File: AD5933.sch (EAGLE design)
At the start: 80 parts, among them U1 ADG1604BRUZ, U10 ADP3303ARZ-3.3, U11 AD5242BRZ1M, U12 AD5245BRJZ100-R2, U2 AD5933YRSZ, U3 AD5242BRZ1M, U4 AD8606ARZ, U5 ADG1604BRUZ, U7 AD8606ARZ, U8 LTC6904MPMS8TRPBF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

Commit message: complete DRC in layout
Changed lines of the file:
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@@
 <class number="0" name="default" width="0" drill="0.3048">
 </class>
-<class number="1" name="power 5v" width="0.508" drill="0.6096">
+<class number="1" name="power 5v" width="0.4064" drill="0.6096">
 </class>
 </classes>
@@
 </nets>
 </sheet>
-<sheet>
-<plain>
-</plain>
-<instances>
-</instances>
-<busses>
-</busses>
-<nets>
-</nets>
-</sheet>

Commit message: Modify top silk screen, estimate wirelength
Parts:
- renumbered ANALOG_PWR to APWR, DIGITAL_PWR to DPWR, JP1 to Z, JP4 to PWR_SEL

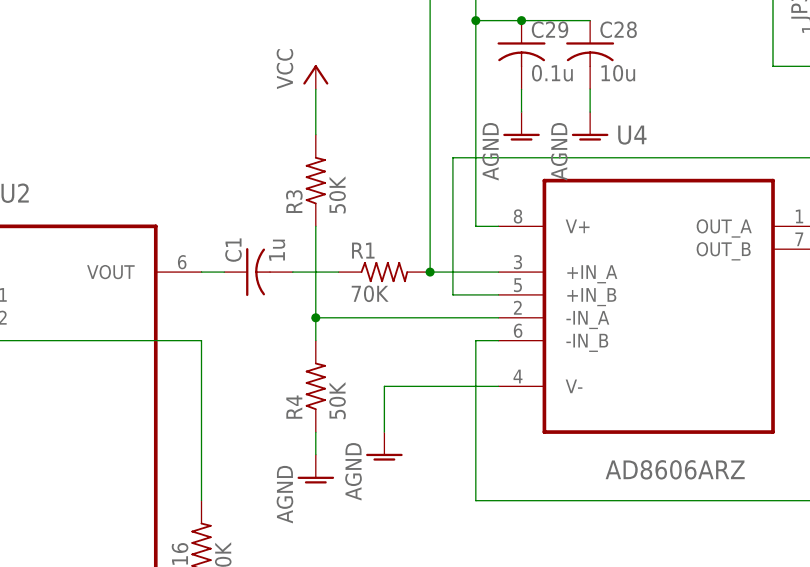
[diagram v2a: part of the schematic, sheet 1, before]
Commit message: Fix ad8606 wiring bug rev 1.1
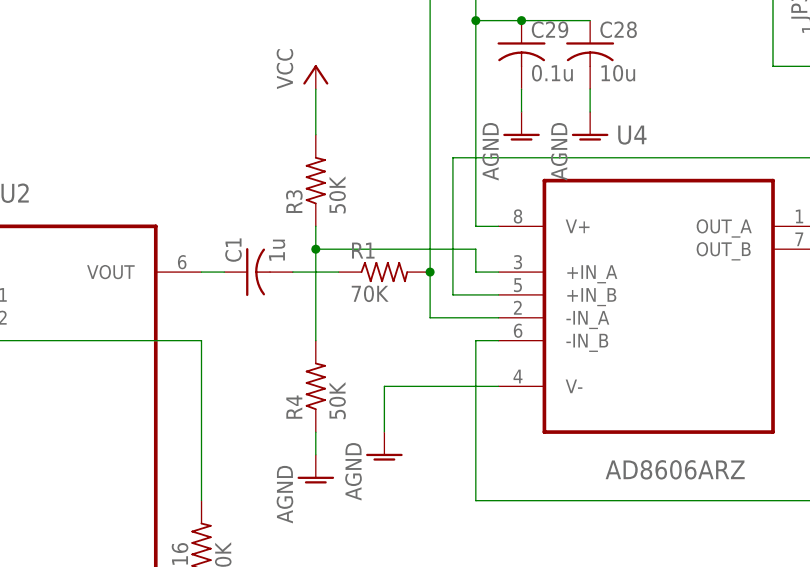
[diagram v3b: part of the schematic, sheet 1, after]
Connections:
- removed net U4_INA+: JP2.2, R1.2, U4.+IN_A
- removed net U4_INA-: R3.1, R4.2, U4.-IN_A
- new net U4_INA++: R3.1, R4.2, U4.+IN_A
- new net U4_INA--: JP2.2, R1.2, U4.-IN_A
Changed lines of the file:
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@@
 </segment>
 </net>
-<net name="U4_INA-" class="0">
+<net name="U4_INA++" class="0">
 <segment>
 <pinref part="R3" gate="G$1" pin="1"/>
-<wire x1="99.06" y1="38.1" x2="99.06" y2="48.26" width="0.1524" layer="91"/>
-<pinref part="U4" gate="A" pin="-IN_A"/>
-<wire x1="99.06" y1="38.1" x2="119.38" y2="38.1" width="0.1524" layer="91"/>
+<wire x1="99.06" y1="35.56" x2="99.06" y2="45.72" width="0.1524" layer="91"/>
 <pinref part="R4" gate="G$1" pin="2"/>
-<wire x1="99.06" y1="38.1" x2="99.06" y2="35.56" width="0.1524" layer="91"/>
-<junction x="99.06" y="38.1"/>
+<wire x1="99.06" y1="45.72" x2="99.06" y2="48.26" width="0.1524" layer="91"/>
+<wire x1="99.06" y1="45.72" x2="116.84" y2="45.72" width="0.1524" layer="91"/>
+<junction x="99.06" y="45.72"/>
+<wire x1="116.84" y1="45.72" x2="116.84" y2="43.18" width="0.1524" layer="91"/>
+<pinref part="U4" gate="A" pin="+IN_A"/>
+<wire x1="116.84" y1="43.18" x2="119.38" y2="43.18" width="0.1524" layer="91"/>
 </segment>
 </net>
@@
 </segment>
 </net>
-<net name="U4_INA+" class="0">
-<segment>
-<pinref part="U4" gate="A" pin="+IN_A"/>
+<net name="U4_INA--" class="0">
+<segment>
 <pinref part="R1" gate="G$1" pin="2"/>
-<wire x1="111.76" y1="43.18" x2="119.38" y2="43.18" width="0.1524" layer="91"/>
 <wire x1="111.76" y1="83.82" x2="111.76" y2="43.18" width="0.1524" layer="91"/>
+<pinref part="JP2" gate="1" pin="2"/>
+<wire x1="111.76" y1="43.18" x2="111.76" y2="38.1" width="0.1524" layer="91"/>
 <junction x="111.76" y="43.18"/>
-<pinref part="JP2" gate="1" pin="2"/>
-</segment>
-</net>
+<pinref part="U4" gate="A" pin="-IN_A"/>
+<wire x1="111.76" y1="38.1" x2="119.38" y2="38.1" width="0.1524" layer="91"/>
+</segment>
+</net>

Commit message: Increase AD5933 pad length
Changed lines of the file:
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@@
+</nets>
+</sheet>
+<sheet>
+<plain>
+</plain>
+<instances>
+</instances>
+<busses>
+</busses>
+<nets>
 </nets>
 </sheet>

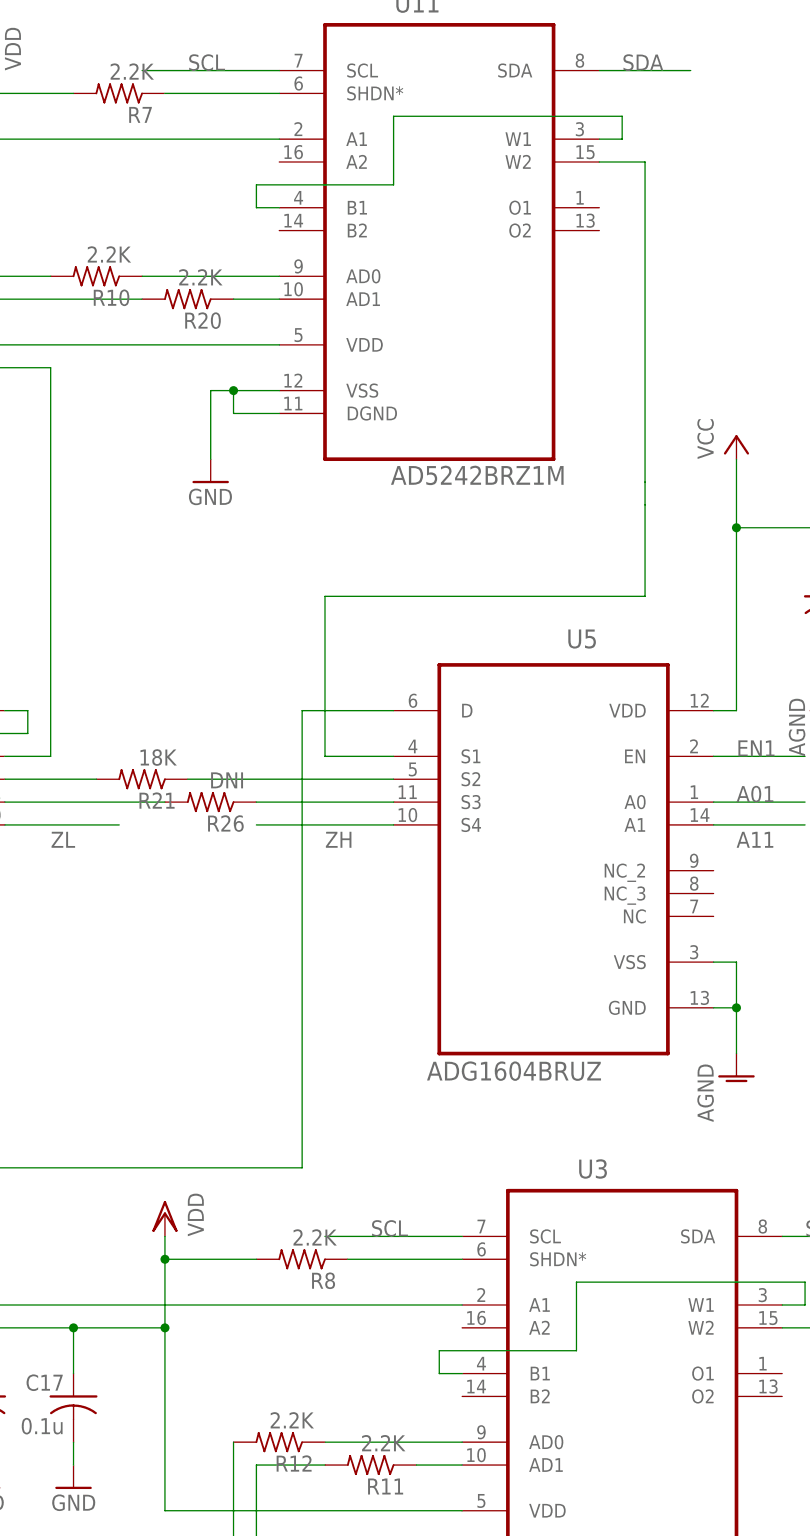
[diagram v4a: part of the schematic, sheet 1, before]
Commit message: Fixed ad5242 open ckt bug, rev 1.2
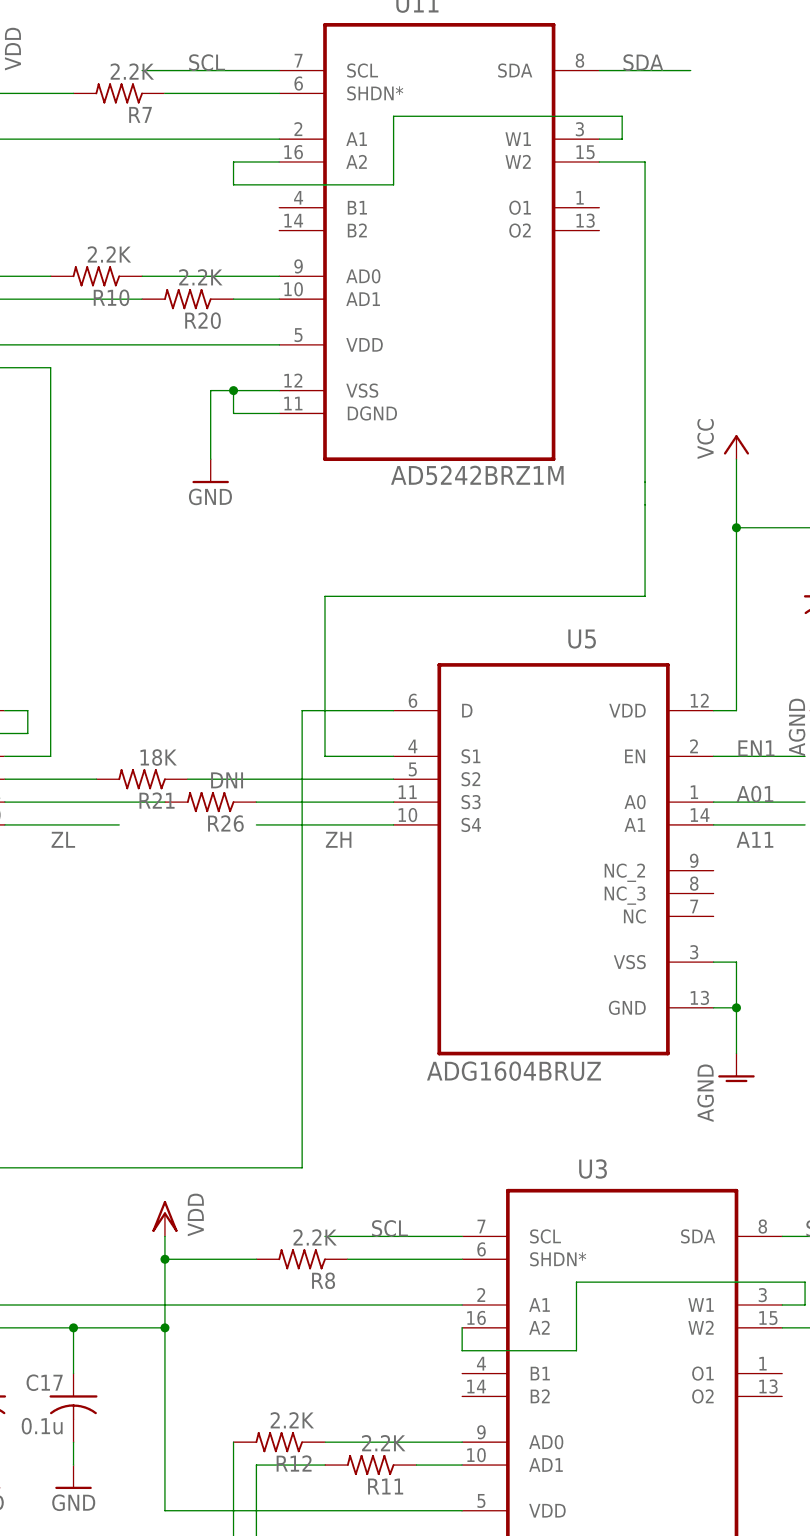
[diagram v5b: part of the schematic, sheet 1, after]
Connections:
- net U11_W1: now also U11.A2; no longer U11.B1
- net U3_W1: now also U3.A2; no longer U3.B1
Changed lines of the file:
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@@
 <wire x1="307.34" y1="-20.32" x2="281.94" y2="-20.32" width="0.1524" layer="91"/>
 <wire x1="281.94" y1="-20.32" x2="281.94" y2="-27.94" width="0.1524" layer="91"/>
-<wire x1="281.94" y1="-27.94" x2="266.7" y2="-27.94" width="0.1524" layer="91"/>
-<wire x1="266.7" y1="-27.94" x2="266.7" y2="-30.48" width="0.1524" layer="91"/>
-<pinref part="U3" gate="A" pin="B1"/>
-<wire x1="266.7" y1="-30.48" x2="269.24" y2="-30.48" width="0.1524" layer="91"/>
+<pinref part="U3" gate="A" pin="A2"/>
+<wire x1="281.94" y1="-27.94" x2="269.24" y2="-27.94" width="0.1524" layer="91"/>
+<wire x1="269.24" y1="-27.94" x2="269.24" y2="-25.4" width="0.1524" layer="91"/>
 </segment>
 </net>
@@
 <wire x1="287.02" y1="109.22" x2="261.62" y2="109.22" width="0.1524" layer="91"/>
 <wire x1="261.62" y1="109.22" x2="261.62" y2="101.6" width="0.1524" layer="91"/>
-<wire x1="261.62" y1="101.6" x2="246.38" y2="101.6" width="0.1524" layer="91"/>
-<wire x1="246.38" y1="101.6" x2="246.38" y2="99.06" width="0.1524" layer="91"/>
-<pinref part="U11" gate="A" pin="B1"/>
-<wire x1="246.38" y1="99.06" x2="248.92" y2="99.06" width="0.1524" layer="91"/>
+<wire x1="261.62" y1="101.6" x2="243.84" y2="101.6" width="0.1524" layer="91"/>
+<pinref part="U11" gate="A" pin="A2"/>
+<wire x1="248.92" y1="104.14" x2="243.84" y2="104.14" width="0.1524" layer="91"/>
+<wire x1="243.84" y1="104.14" x2="243.84" y2="101.6" width="0.1524" layer="91"/>
 </segment>
 </net>

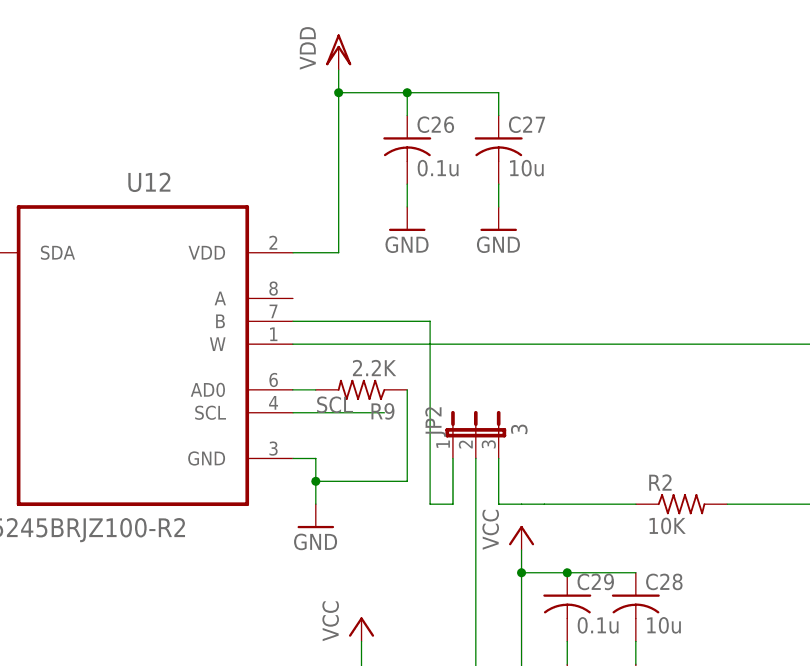
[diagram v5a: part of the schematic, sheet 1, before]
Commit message: fix ad5245 address to 0x2d to remove iic bus conflict with ad5242-u3
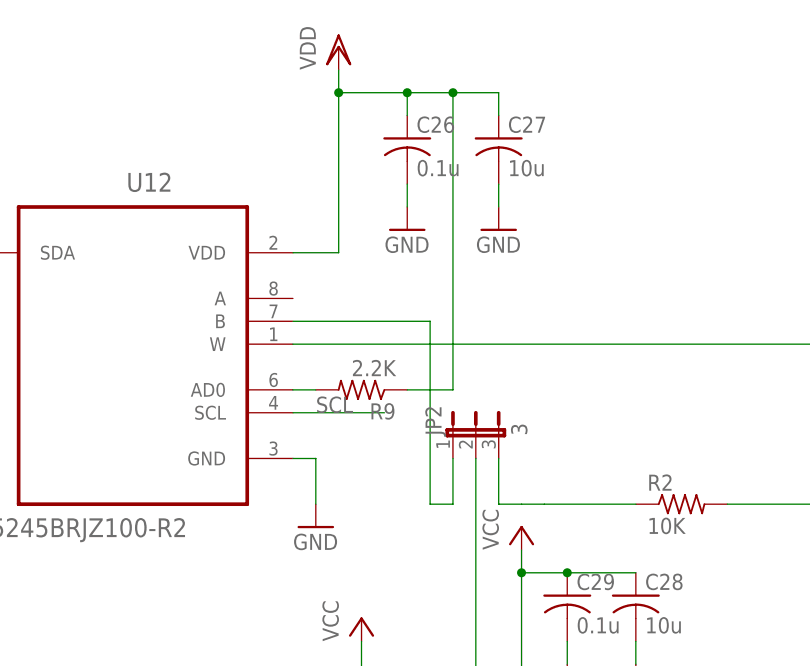
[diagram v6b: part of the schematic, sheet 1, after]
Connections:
- net GND: no longer R9.1
- net VDD: now also R9.1
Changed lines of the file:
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@@
 <junction x="96.52" y="124.46"/>
 <pinref part="C27" gate="G$1" pin="1"/>
-<wire x1="104.14" y1="124.46" x2="114.3" y2="124.46" width="0.1524" layer="91"/>
+<wire x1="104.14" y1="124.46" x2="109.22" y2="124.46" width="0.1524" layer="91"/>
+<wire x1="109.22" y1="124.46" x2="114.3" y2="124.46" width="0.1524" layer="91"/>
 <wire x1="114.3" y1="124.46" x2="114.3" y2="121.92" width="0.1524" layer="91"/>
 <junction x="104.14" y="124.46"/>
+<pinref part="R9" gate="G$1" pin="1"/>
+<wire x1="104.14" y1="91.44" x2="109.22" y2="91.44" width="0.1524" layer="91"/>
+<wire x1="109.22" y1="91.44" x2="109.22" y2="124.46" width="0.1524" layer="91"/>
+<junction x="109.22" y="124.46"/>
 </segment>
 <segment>
@@
 <wire x1="91.44" y1="83.82" x2="93.98" y2="83.82" width="0.1524" layer="91"/>
 <pinref part="GND12" gate="1" pin="GND"/>
-<wire x1="93.98" y1="78.74" x2="93.98" y2="81.28" width="0.1524" layer="91"/>
-<pinref part="R9" gate="G$1" pin="1"/>
-<wire x1="93.98" y1="81.28" x2="93.98" y2="83.82" width="0.1524" layer="91"/>
-<wire x1="104.14" y1="91.44" x2="104.14" y2="81.28" width="0.1524" layer="91"/>
-<wire x1="104.14" y1="81.28" x2="93.98" y2="81.28" width="0.1524" layer="91"/>
-<junction x="93.98" y="81.28"/>
-</segment>
-<segment>
+<wire x1="93.98" y1="78.74" x2="93.98" y2="83.82" width="0.1524" layer="91"/>
+</segment>
+<segment>
